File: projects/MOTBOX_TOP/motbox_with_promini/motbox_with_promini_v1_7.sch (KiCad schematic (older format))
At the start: 25 parts, among them J1 JST_XH_2pin, J2 JST_XH_3pin, J3 Conn_01x02, J4 JST_XH_4pin, J5 JST_XH_3pin, J6 JST_XH_3pin, J7 JST_XH_2pin, U1 LM2576R-5.0, U2 L293D

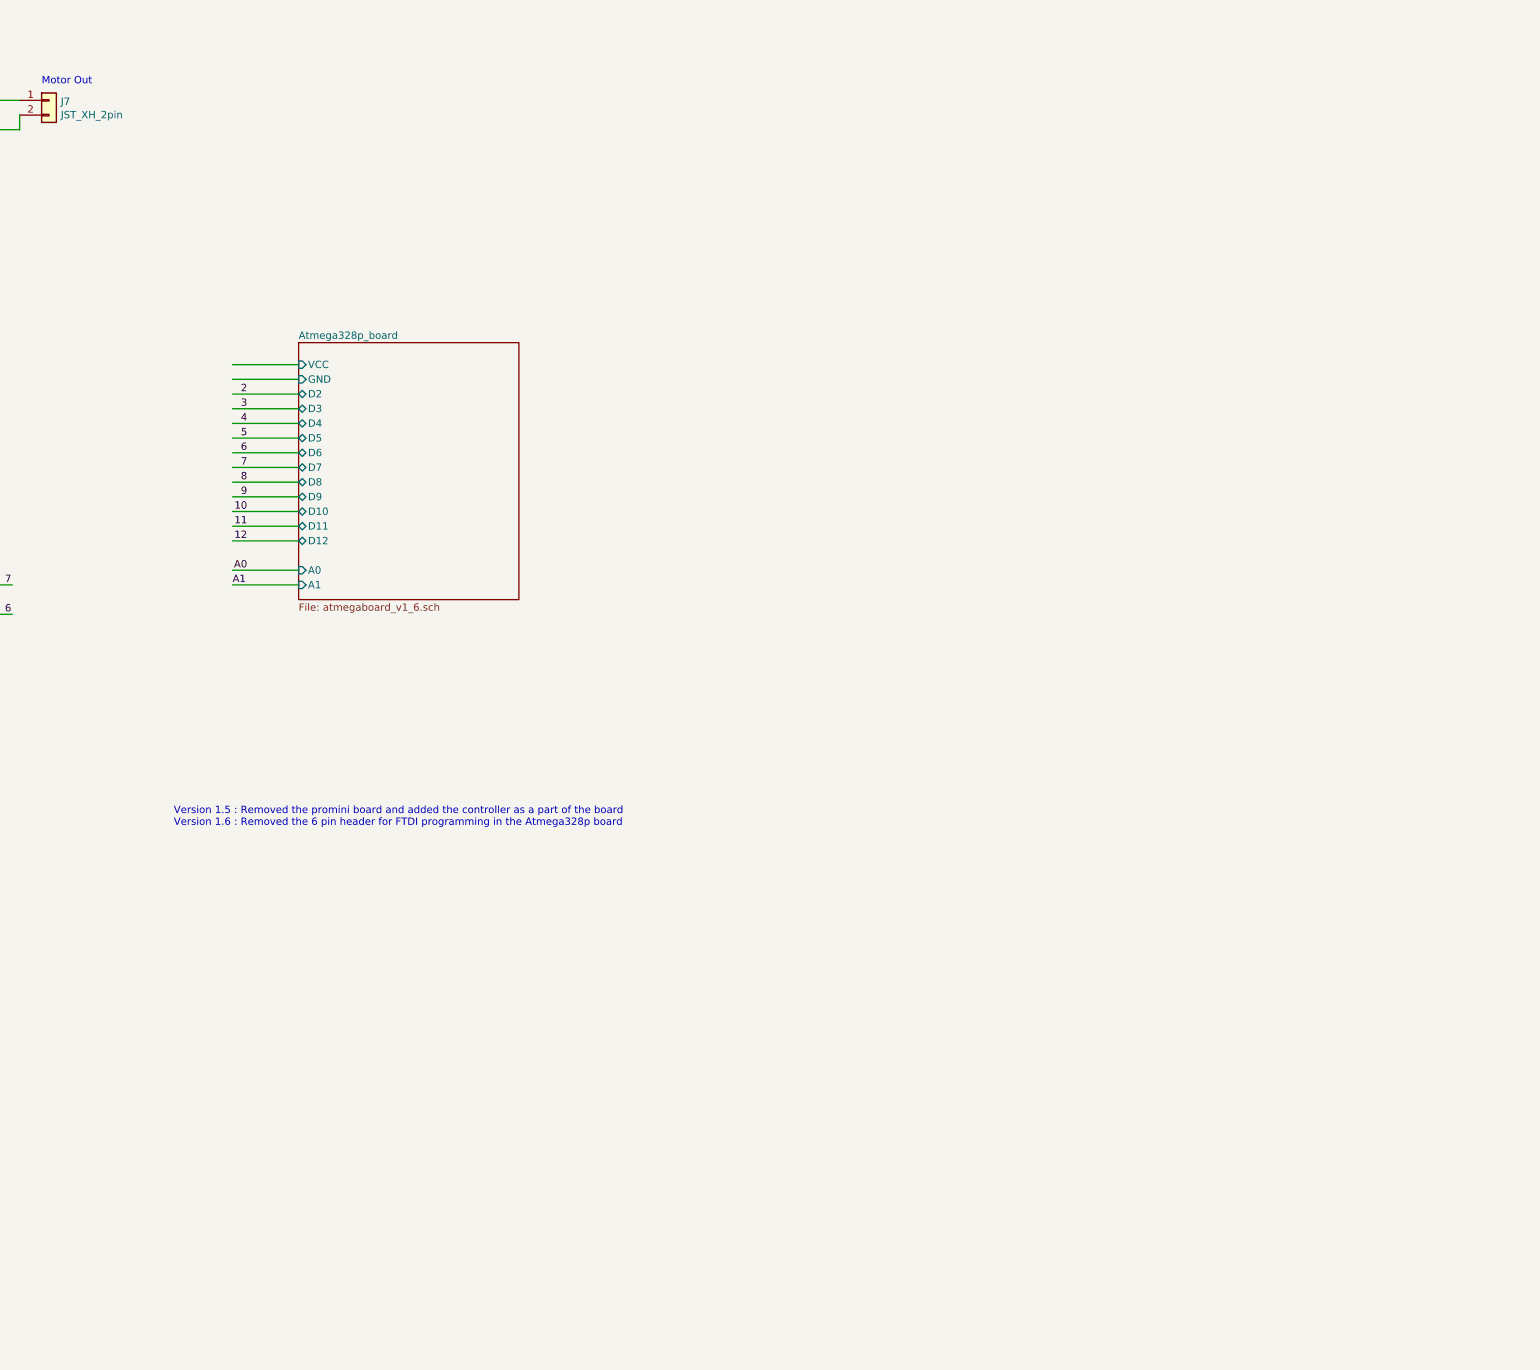
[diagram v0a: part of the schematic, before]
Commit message: For transparent cable detection
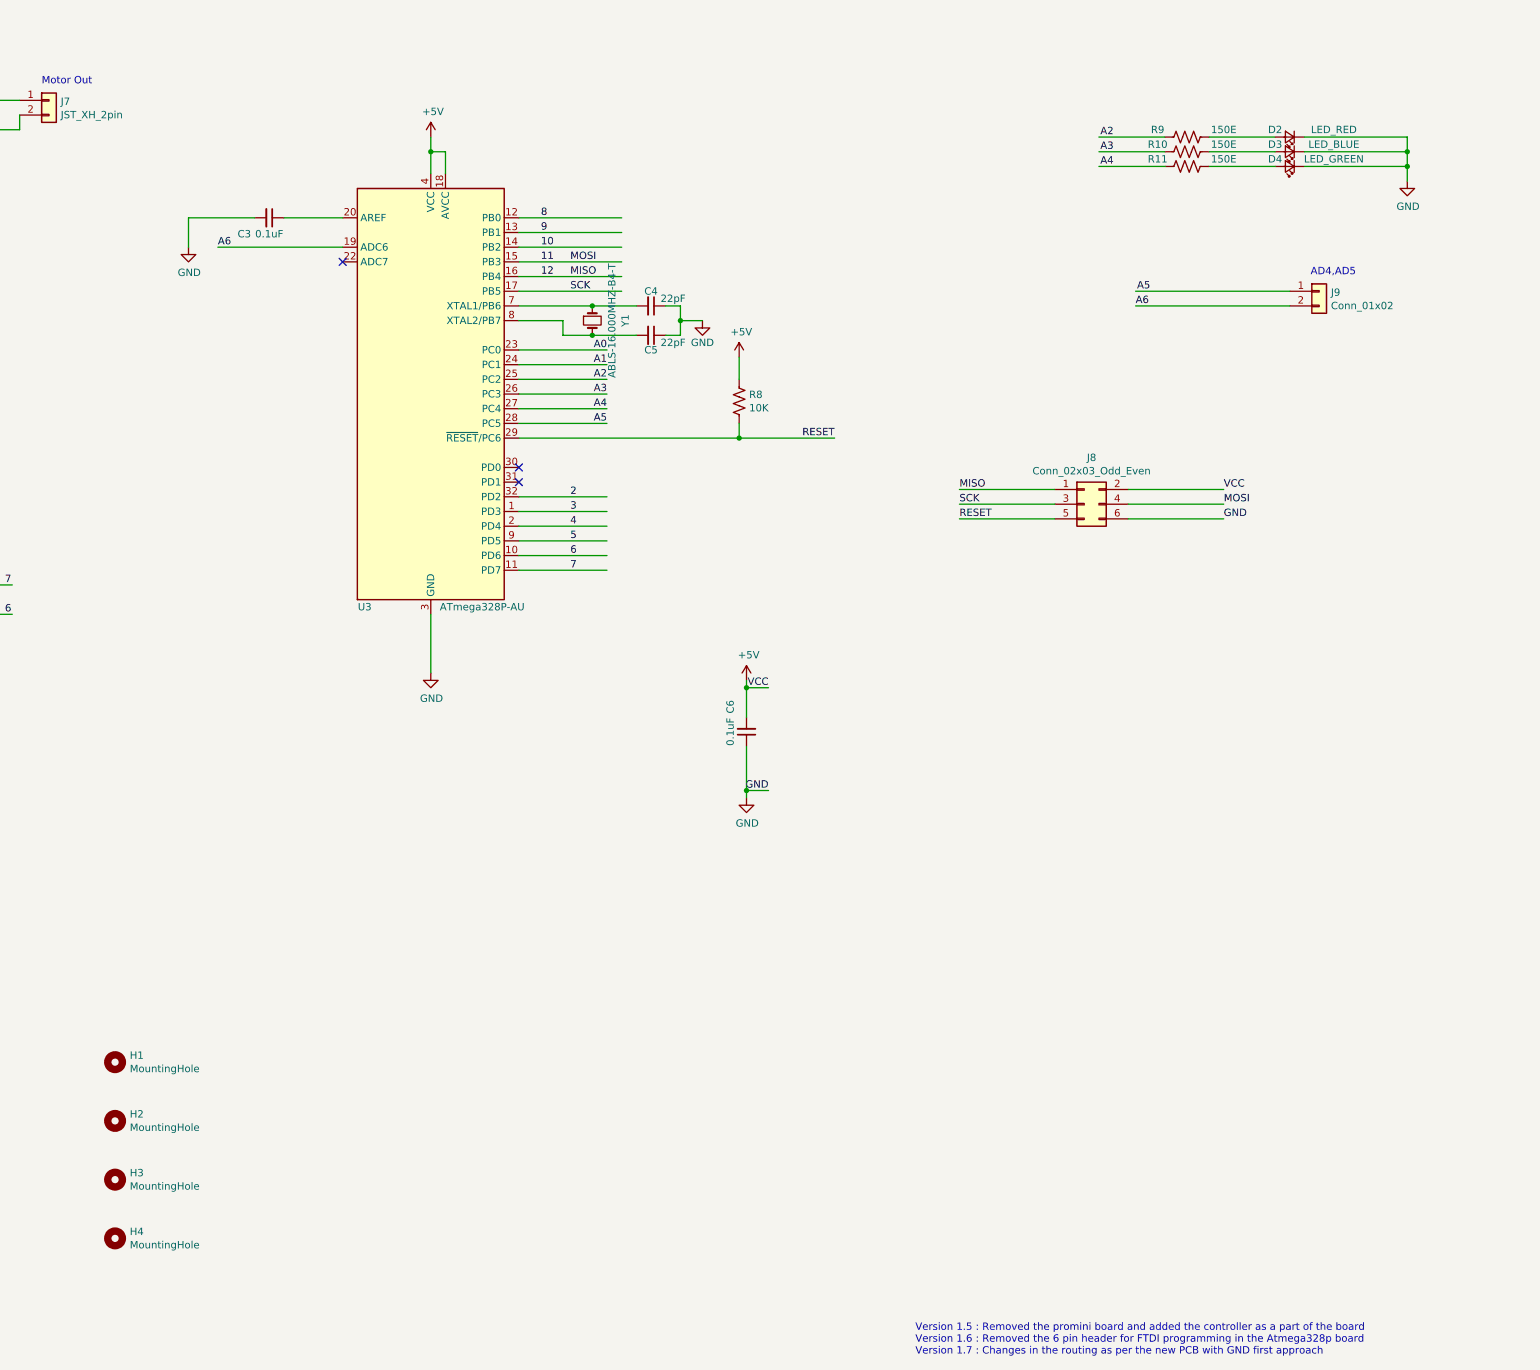
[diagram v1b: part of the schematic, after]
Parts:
- added C3, C6: 0.1uF, Capacitor_SMD:C_0603_1608Metric, symbol Device:C_Small
- added C4, C5: 22pF, Capacitor_SMD:C_0603_1608Metric, symbol Device:C_Small
- added D2: LED_RED, LED_SMD:LED_0603_1608Metric, symbol Device:LED_Small
- added D3: LED_BLUE, LED_SMD:LED_0603_1608Metric, symbol Device:LED_Small
- added D4: LED_GREEN, LED_SMD:LED_0603_1608Metric, symbol Device:LED_Small
- added H1, H2, H3, H4: MountingHole, MountingHole:MountingHole_2.2mm_M2_ISO7380, symbol Mechanical:MountingHole
- added J8: Conn_02x03_Odd_Even, Connector_PinHeader_2.54mm:PinHeader_2x03_P2.54mm_Vertical, symbol Connector_Generic:Conn_02x03_Odd_Even
- added J9: Conn_01x02, Connector_PinHeader_2.54mm:PinHeader_1x02_P2.54mm_Vertical, symbol Connector_Generic:Conn_01x02
- added R10, R11, R9: 150E, Resistor_SMD:R_0603_1608Metric, symbol Device:R_US
- added R8: 10K, Resistor_SMD:R_0603_1608Metric, symbol Device:R_US
- added U3: ATmega328P-AU, Package_QFP:TQFP-32_7x7mm_P0.8mm, symbol MCU_Microchip_ATmega:ATmega328P-AU
- added Y1: ABLS-16.000MHZ-B4-T, Crystal:Crystal_SMD_HC49-SD, symbol Device:Crystal_Small
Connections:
- net labels added: A2, A3, A4, A5, A6, MISO, MOSI, RESET, SCK
- wire segments 108 -> 161
- no-connect marks 4 -> 7
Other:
- note added: "AD4,AD5"
- note added: "Version 1.5 : Removed the promini board and added the controller as a part of the board\nVersion 1.6 : Removed the 6 pin header for FTDI programming in the Atmega328p board\nVersion 1.7 : Changes in the routing as per the new PCB with GND first approach"
- note removed: "Version 1.5 : Removed the promini board and added the controller as a part of the board\nVersion 1.6 : Removed the 6 pin header for FTDI programming in the Atmega328p board"
